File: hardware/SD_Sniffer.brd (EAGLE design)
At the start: 73.7 x 34.8 mm, 10 parts, among them U1 SD_CARD_SOCKET4UCON, U2 SD_MMC_CARDSD_PCB

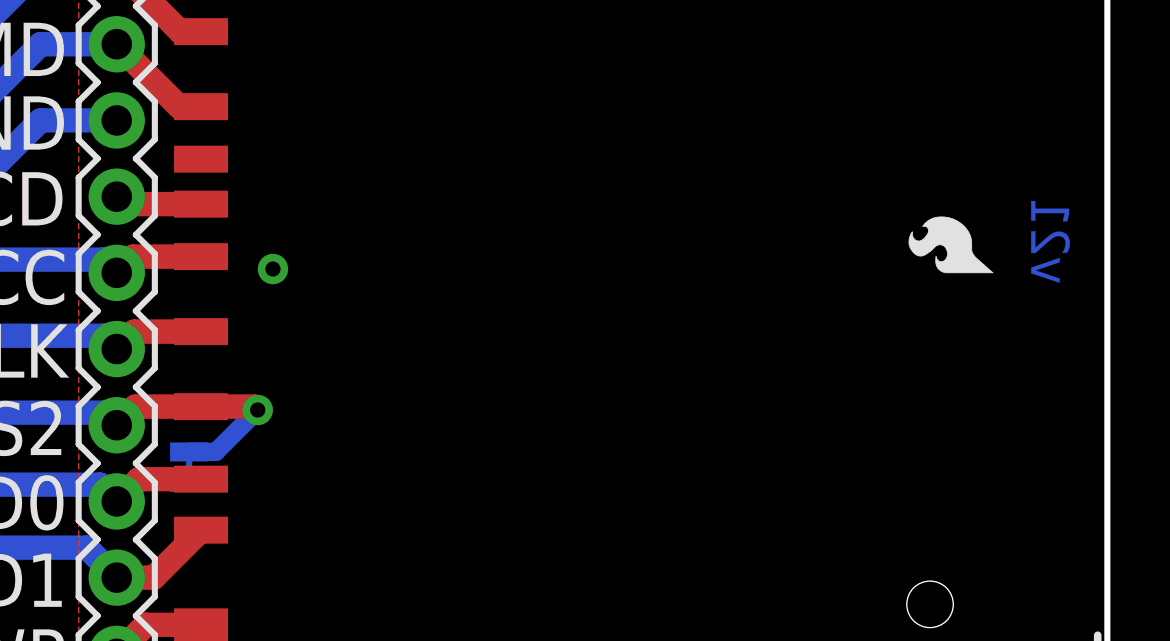
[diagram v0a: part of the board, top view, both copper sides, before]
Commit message: Moved via, Added Bigger Flame, Named Jumper
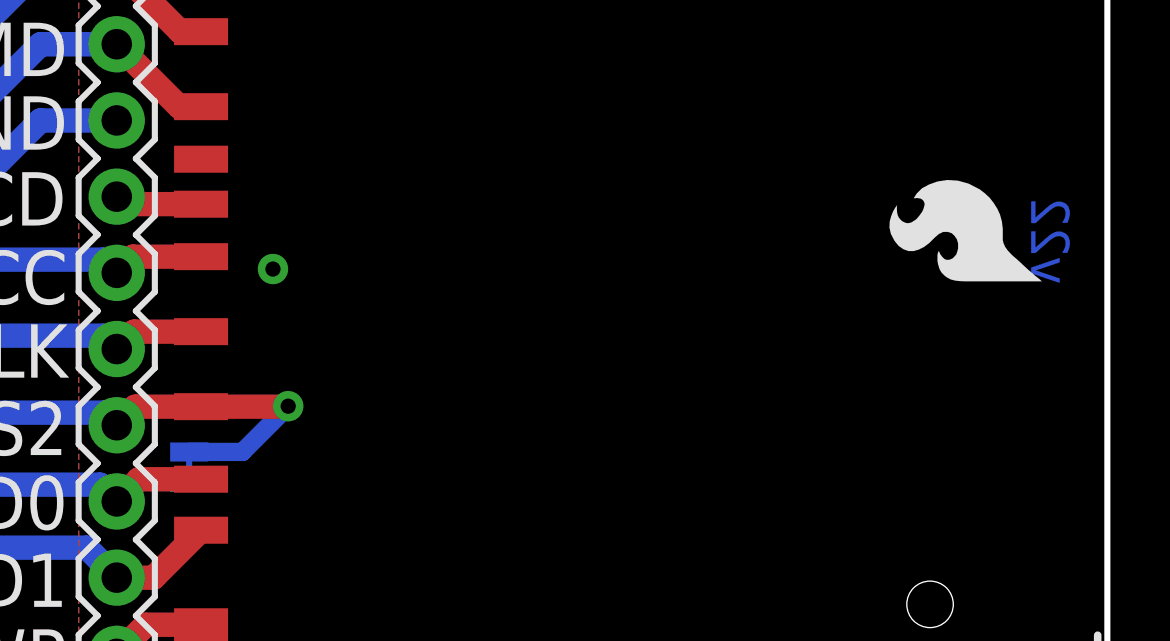
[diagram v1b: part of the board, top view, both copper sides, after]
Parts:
- removed U$1: CREATIVE_COMMONS, SparkFun-Aesthetics:CREATIVE_COMMONS
- added FRAME1: FRAME-LETTER, SparkFun-Aesthetics:CREATIVE_COMMONS
- U$4: value LOGO-SFESK -> SFE_LOGO_FLAME.2_INCH; device SparkFun:SFE-LOGO-FLAME -> SparkFun-Aesthetics:SFE_LOGO_FLAME_.2
- moved U$4 2.01 mm to (71.8, 14.6)
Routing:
- net VSS2: track 45.6 -> 47.6 mm
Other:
- board text added: "Aaron Weiss"
- board text added: "Revised by: Patrick Alberts"
- board text added: "v22"
- board text removed: "v21"

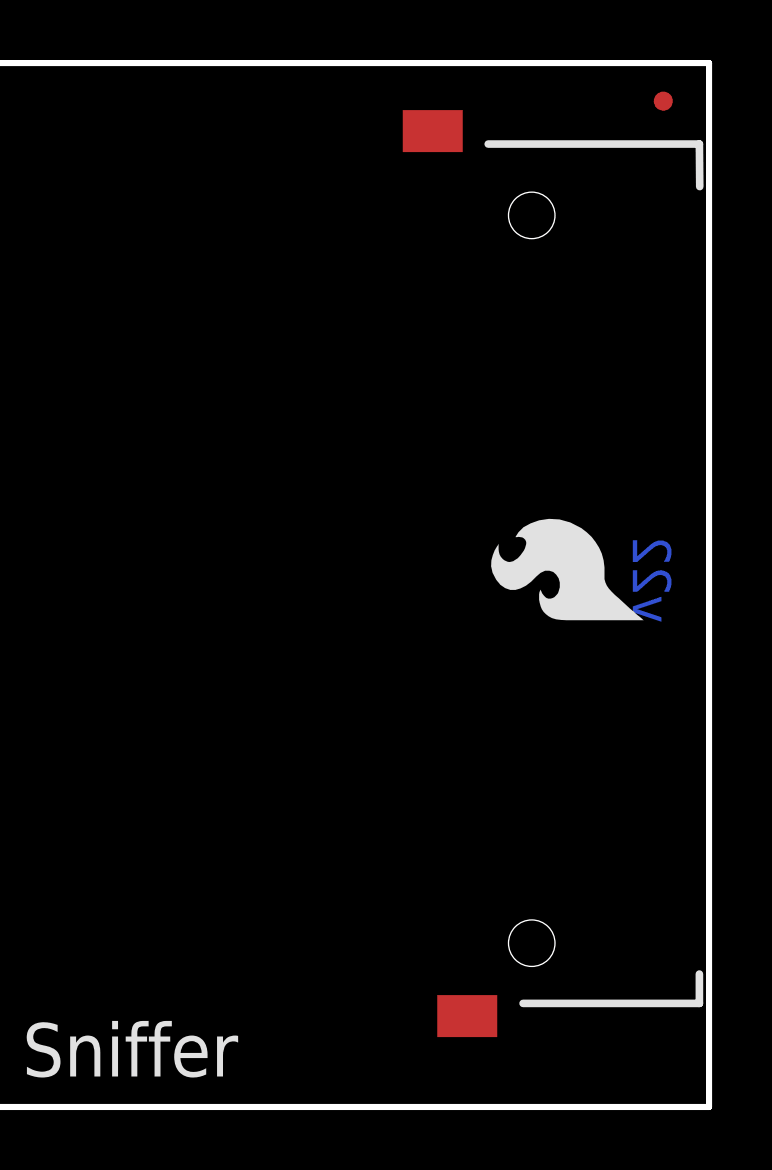
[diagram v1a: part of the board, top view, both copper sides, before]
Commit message: Added updated SD socket
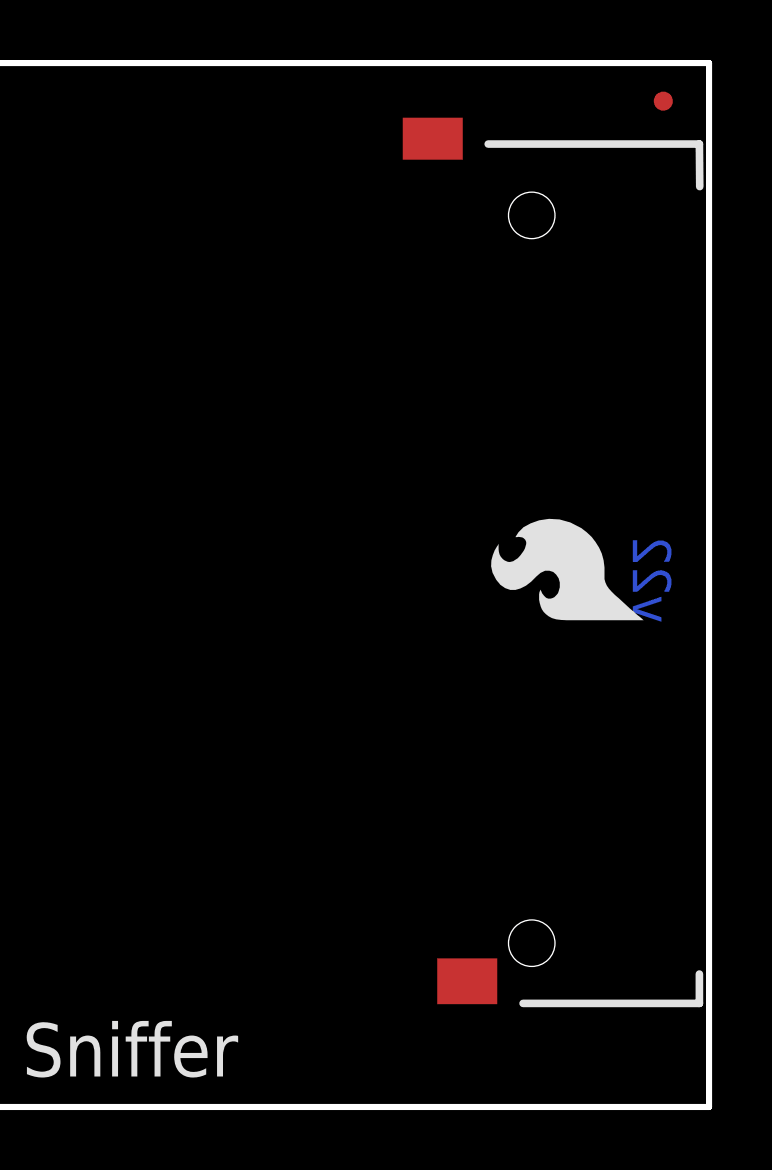
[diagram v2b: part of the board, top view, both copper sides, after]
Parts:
- U1: value SD_CARD_SOCKET4UCON -> SD_CARD_SOCKET; device SparkFun-Connectors:SDCARD_4UCONN -> SparkFun-Connectors:SD_1:1
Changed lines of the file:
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@@
 <setting verticaltext="up"/>
 </settings>
-<grid distance="0.05" unitdist="inch" unit="inch" style="lines" multiple="1" display="yes" altdistance="0.001" altunitdist="inch" altunit="inch"/>
+<grid distance="0.05" unitdist="inch" unit="inch" style="lines" multiple="1" display="yes" altdistance="0.005" altunitdist="inch" altunit="inch"/>
 <layers>
 <layer number="1" name="Top" color="4" fill="1" visible="yes" active="yes"/>
@@
 <layer number="27" name="tValues" color="7" fill="1" visible="no" active="yes"/>
 <layer number="28" name="bValues" color="7" fill="1" visible="no" active="yes"/>
-<layer number="29" name="tStop" color="7" fill="3" visible="no" active="yes"/>
+<layer number="29" name="tStop" color="7" fill="3" visible="yes" active="yes"/>
 <layer number="30" name="bStop" color="7" fill="6" visible="no" active="yes"/>
 <layer number="31" name="tCream" color="7" fill="4" visible="no" active="yes"/>
@@
 <layer number="108" name="tplace-old" color="10" fill="1" visible="no" active="yes"/>
 <layer number="109" name="ref-old" color="11" fill="1" visible="no" active="yes"/>
-<layer number="110" name="fp0" color="7" fill="1" visible="yes" active="yes"/>
-<layer number="111" name="LPC17xx" color="7" fill="1" visible="yes" active="yes"/>
-<layer number="112" name="tSilk" color="7" fill="1" visible="yes" active="yes"/>
-<layer number="113" name="IDFDebug" color="4" fill="1" visible="yes" active="yes"/>
+<layer number="110" name="fp0" color="7" fill="1" visible="no" active="yes"/>
+<layer number="111" name="LPC17xx" color="7" fill="1" visible="no" active="yes"/>
+<layer number="112" name="tSilk" color="7" fill="1" visible="no" active="yes"/>
+<layer number="113" name="IDFDebug" color="4" fill="1" visible="no" active="yes"/>
 <layer number="116" name="Patch_BOT" color="9" fill="4" visible="no" active="yes"/>
 <layer number="121" name="_tsilk" color="7" fill="1" visible="no" active="yes"/>
 <layer number="122" name="_bsilk" color="7" fill="1" visible="no" active="yes"/>
-<layer number="123" name="tTestmark" color="7" fill="1" visible="yes" active="yes"/>
-<layer number="124" name="bTestmark" color="7" fill="1" visible="yes" active="yes"/>
+<layer number="123" name="tTestmark" color="7" fill="1" visible="no" active="yes"/>
+<layer number="124" name="bTestmark" color="7" fill="1" visible="no" active="yes"/>
 <layer number="125" name="_tNames" color="7" fill="1" visible="no" active="yes"/>
-<layer number="126" name="_bNames" color="7" fill="1" visible="yes" active="yes"/>
-<layer number="127" name="_tValues" color="7" fill="1" visible="yes" active="yes"/>
-<layer number="128" name="_bValues" color="7" fill="1" visible="yes" active="yes"/>
-<layer number="131" name="tAdjust" color="7" fill="1" visible="yes" active="yes"/>
-<layer number="132" name="bAdjust" color="7" fill="1" visible="yes" active="yes"/>
+<layer number="126" name="_bNames" color="7" fill="1" visible="no" active="yes"/>
+<layer number="127" name="_tValues" color="7" fill="1" visible="no" active="yes"/>
+<layer number="128" name="_bValues" color="7" fill="1" visible="no" active="yes"/>
+<layer number="131" name="tAdjust" color="7" fill="1" visible="no" active="yes"/>
+<layer number="132" name="bAdjust" color="7" fill="1" visible="no" active="yes"/>
 <layer number="144" name="Drill_legend" color="7" fill="1" visible="no" active="yes"/>
 <layer number="151" name="HeatSink" color="7" fill="1" visible="no" active="yes"/>
-<layer number="152" name="_bDocu" color="7" fill="1" visible="yes" active="yes"/>
+<layer number="152" name="_bDocu" color="7" fill="1" visible="no" active="yes"/>
 <layer number="199" name="Contour" color="7" fill="1" visible="no" active="yes"/>
 <layer number="200" name="200bmp" color="1" fill="10" visible="no" active="no"/>
@@
 <layer number="223" name="223bmp" color="24" fill="1" visible="no" active="no"/>
 <layer number="224" name="224bmp" color="25" fill="1" visible="no" active="no"/>
-<layer number="248" name="Housing" color="7" fill="1" visible="yes" active="yes"/>
-<layer number="249" name="Edge" color="7" fill="1" visible="yes" active="yes"/>
+<layer number="248" name="Housing" color="7" fill="1" visible="no" active="yes"/>
+<layer number="249" name="Edge" color="7" fill="1" visible="no" active="yes"/>
 <layer number="250" name="Descript" color="3" fill="1" visible="no" active="no"/>
 <layer number="251" name="SMDround" color="12" fill="11" visible="no" active="no"/>
@@
 <element name="LOGO" library="SparkFun" package="SFE-NEW-WEBLOGO" value="LOGO-SFENEW" x="55.753" y="6.604" smashed="yes" rot="MR90"/>
 <element name="U$4" library="SparkFun-Aesthetics" package="SFE_LOGO_FLAME_.2" value="SFE_LOGO_FLAME.2_INCH" x="71.755" y="14.605" smashed="yes" rot="R90"/>
-<element name="U1" library="SparkFun-Connectors" package="SDCARD_4UCONN" value="SD_CARD_SOCKET4UCON" x="44.45" y="16.51" smashed="yes">
+<element name="U1" library="SparkFun-Connectors" package="SD_1:1" value="SD_CARD_SOCKET" x="44.45" y="16.51" smashed="yes">
 <attribute name="NAME" x="44.99" y="29.45" size="0.4064" layer="25"/>
 <attribute name="VALUE" x="44.99" y="28.18" size="0.4064" layer="27"/>

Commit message: Fixed eagle sync
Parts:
- U2: device SparkFun:SD-MMC-CARD@1 -> SparkFun-Boards:SD-MMC-CARD
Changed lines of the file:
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@@
 <layer number="27" name="tValues" color="7" fill="1" visible="no" active="yes"/>
 <layer number="28" name="bValues" color="7" fill="1" visible="no" active="yes"/>
-<layer number="29" name="tStop" color="7" fill="3" visible="yes" active="yes"/>
+<layer number="29" name="tStop" color="7" fill="3" visible="no" active="yes"/>
 <layer number="30" name="bStop" color="7" fill="6" visible="no" active="yes"/>
 <layer number="31" name="tCream" color="7" fill="4" visible="no" active="yes"/>
@@
 </autorouter>
 <elements>
-<element name="U2" library="SparkFun" package="SD-MMC-CARD@1" value="SD_MMC_CARDSD_PCB" x="17.78" y="16.51" smashed="yes" rot="MR270">
+<element name="U2" library="SparkFun-Boards" package="SD-MMC-CARD" value="SD_MMC_CARDSD_PCB" x="17.78" y="16.51" smashed="yes" rot="MR270">
 <attribute name="NAME" x="-1.27" y="21.59" size="0.4064" layer="26" rot="MR90"/>
 <attribute name="VALUE" x="-1.27" y="10.16" size="0.4064" layer="28" rot="MR90"/>
@@
 <wire x1="40.64" y1="27.94" x2="36.83" y2="27.94" width="0.8128" layer="16"/>
 <wire x1="36.83" y1="27.94" x2="35.56" y2="26.67" width="0.8128" layer="16"/>
-<wire x1="5.75" y1="25.94" x2="34.83" y2="25.94" width="0.8128" layer="16"/>
+<wire x1="5.75" y1="26.04" x2="34.83" y2="25.94" width="0.8128" layer="16"/>
 <wire x1="34.83" y1="25.94" x2="35.56" y2="26.67" width="0.8128" layer="16"/>
 </signal>
@@
 <via x="45.847" y="15.367" extent="1-16" drill="0.508"/>
 <contactref element="JP4" pad="4"/>
-<wire x1="3.077" y1="18.21" x2="35.99" y2="18.21" width="0.8128" layer="16"/>
+<wire x1="3.077" y1="18.11" x2="35.99" y2="18.21" width="0.8128" layer="16"/>
 <wire x1="35.99" y1="18.21" x2="38.1" y2="20.32" width="0.8128" layer="16"/>
 <wire x1="38.1" y1="20.32" x2="40.64" y2="20.32" width="0.8128" layer="16"/>
@@
 <contactref element="U1" pad="5"/>
 <contactref element="JP4" pad="7"/>
-<wire x1="3.077" y1="13.145" x2="40.195" y2="13.145" width="0.8128" layer="16"/>
+<wire x1="3.077" y1="13.045" x2="40.195" y2="13.145" width="0.8128" layer="16"/>
 <wire x1="40.195" y1="13.145" x2="40.64" y2="12.7" width="0.8128" layer="16"/>
 <wire x1="43.45" y1="13.28" x2="41.22" y2="13.28" width="0.8128" layer="1"/>
@@
 <contactref element="U1" pad="7"/>
 <contactref element="JP4" pad="9"/>
-<wire x1="3.077" y1="8.18" x2="40.08" y2="8.18" width="0.8128" layer="16"/>
+<wire x1="3.077" y1="8.08" x2="40.08" y2="8.18" width="0.8128" layer="16"/>
 <wire x1="40.08" y1="8.18" x2="40.64" y2="7.62" width="0.8128" layer="16"/>
 <wire x1="43.45" y1="8.36" x2="41.38" y2="8.36" width="0.8128" layer="1"/>
@@
 <contactref element="U2" pad="4"/>
 <contactref element="JP4" pad="6"/>
-<wire x1="3.077" y1="15.68" x2="40.2" y2="15.68" width="0.8128" layer="16"/>
+<wire x1="3.077" y1="15.58" x2="40.2" y2="15.68" width="0.8128" layer="16"/>
 <wire x1="40.2" y1="15.68" x2="40.64" y2="15.24" width="0.8128" layer="16"/>
 <wire x1="43.45" y1="15.78" x2="41.18" y2="15.78" width="0.8128" layer="1"/>
@@
 <contactref element="SJ1" pad="2"/>
 <contactref element="JP4" pad="8"/>
-<wire x1="3.077" y1="10.58" x2="40.22" y2="10.58" width="0.8128" layer="16"/>
+<wire x1="3.077" y1="10.48" x2="40.22" y2="10.58" width="0.8128" layer="16"/>
 <wire x1="40.22" y1="10.58" x2="40.64" y2="10.16" width="0.8128" layer="16"/>
 <wire x1="43.45" y1="10.78" x2="41.26" y2="10.78" width="0.8128" layer="1"/>
